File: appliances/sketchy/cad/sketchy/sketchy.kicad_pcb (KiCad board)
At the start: 2 copper layers, 6 parts, among them J1 Barrel_Jack, M1 Stepper_Motor_bipolar, M2 Stepper_Motor_bipolar, U1 ESP32PICO-KIT

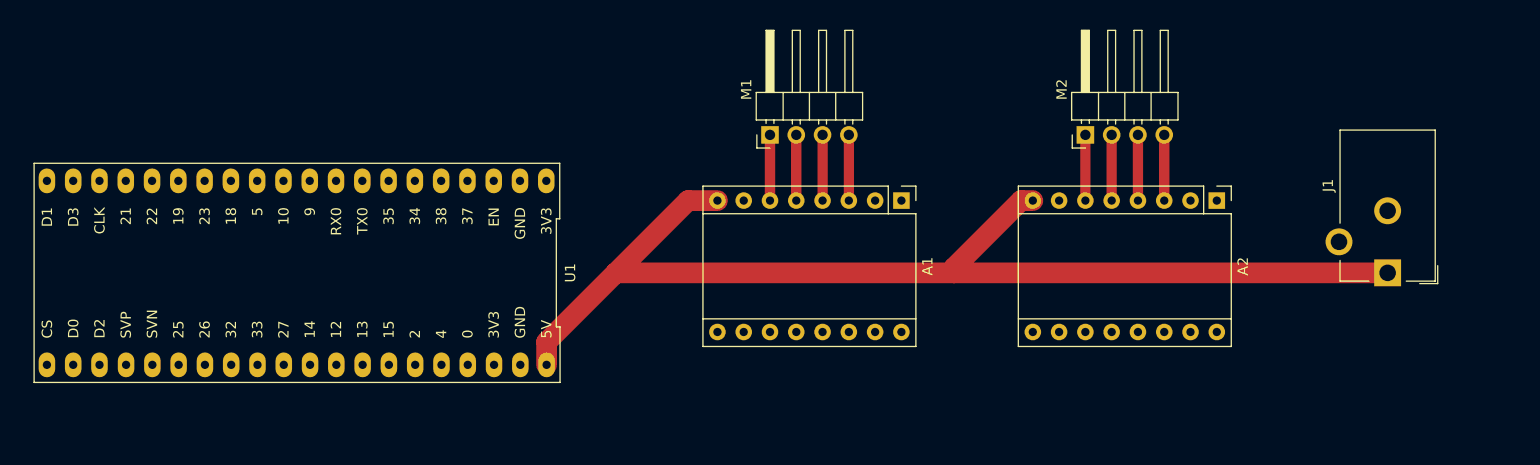
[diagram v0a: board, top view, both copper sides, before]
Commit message: Changed stepper driver to the 4988 that I'm actually using, routed all tracks, and added silkscreen text and mounting holes.
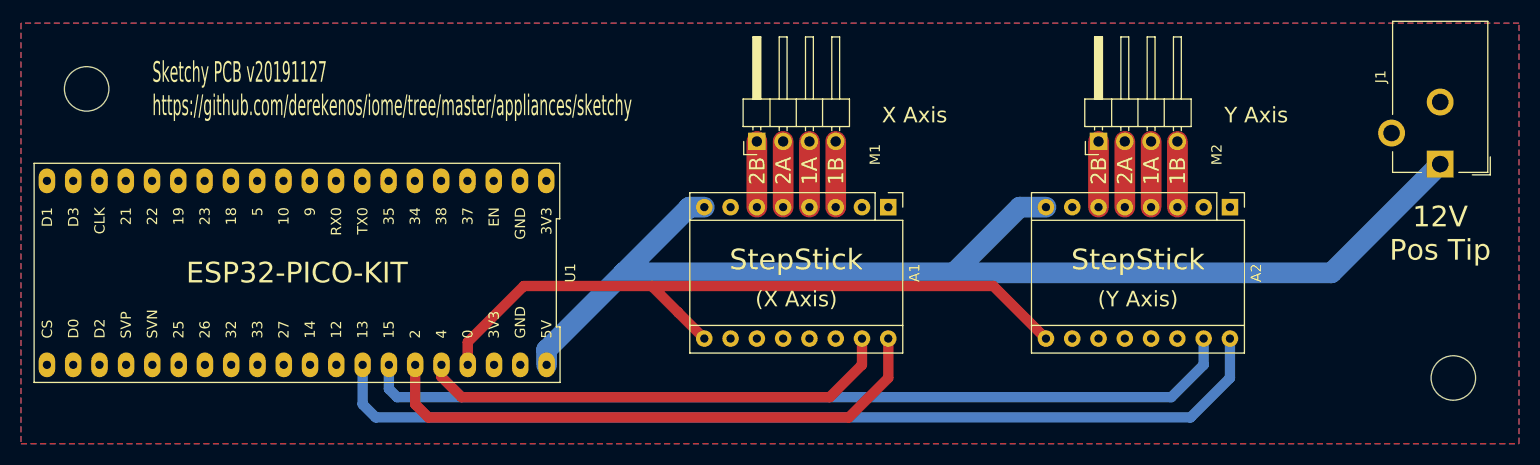
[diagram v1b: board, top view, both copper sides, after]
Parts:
- added REF**: MountingHole_4.3mm_M4, Mounting_Holes:MountingHole_4.3mm_M4, F.Cu at (195.6, 86.4)
- added REF**: MountingHole_4.3mm_M4, Mounting_Holes:MountingHole_4.3mm_M4, F.Cu at (63.5, 58.4)
- A1, A2: value Pololu_Breakout_DRV8825 -> Pololu_Breakout_A4988
- U1: value ESP32PICO-KIT -> ESP32-PICO-KIT
- moved J1 11.7 mm to (194.3, 65.7)
- moved A1 1.42 mm to (141.0, 69.8)
- moved A2 1.42 mm to (174.0, 69.8)
- moved M1 1.42 mm to (128.3, 63.5)
- moved M2 1.42 mm to (161.3, 63.5)
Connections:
- U1 pad 33: NOT_ENABLE -> STEPPER_Y_DIR
- U1 pad 34: STEPPER_X_STEP -> STEPPER_Y_STEP
- U1 pad 36: STEPPER_Y_STEP -> STEPPER_X_STEP
- U1 pad 37: STEPPER_Y_DIR -> NOT_ENABLE
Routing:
- net STEPPER_Y_DIR: track 0.00 -> 93.5 mm
- net STEPPER_Y_STEP: track 0.00 -> 85.2 mm
- net NOT_ENABLE: track 0.00 -> 69.6 mm
- net STEPPER_X_DIR: track 0.00 -> 55.4 mm
- net STEPPER_X_STEP: track 0.00 -> 46.5 mm
- net VDD: track 109.8 -> 117.2 mm
- added copper zone on B.Cu, net 3V3
- added copper zone on F.Cu, net GND
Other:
- board text added: "(X Axis)"
- board text added: "(Y Axis)"
- board text added: "12V Pos Tip"
- board text added: "1A"
- board text added: "1B"
- board text added: "2A"
- board text added: "2B"
- board text added: "Sketchy PCB v20191127 https://github.com/derekenos/iome/tree/master/appliances/sketchy"
- board text added: "StepStick"
- board text added: "X Axis"
- board text added: "Y Axis"

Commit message: Created denser (v2) PCB
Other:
- board outline added: 144.8 x 40.6 mm
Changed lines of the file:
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@@
   (general
     (thickness 1.6)
-    (drawings 16)
+    (drawings 20)
     (tracks 46)
     (modules 8)
@@
   (layers
     (0 "F.Cu" signal)
-    (31 "B.Cu" signal)
-    (32 "B.Adhes" user)
-    (33 "F.Adhes" user)
-    (34 "B.Paste" user)
-    (35 "F.Paste" user)
-    (36 "B.SilkS" user)
-    (37 "F.SilkS" user)
-    (38 "B.Mask" user)
-    (39 "F.Mask" user)
-    (40 "Dwgs.User" user)
-    (41 "Cmts.User" user)
-    (42 "Eco1.User" user)
-    (43 "Eco2.User" user)
+    (31 "B.Cu" signal hide)
+    (32 "B.Adhes" user hide)
+    (33 "F.Adhes" user hide)
+    (34 "B.Paste" user hide)
+    (35 "F.Paste" user hide)
+    (36 "B.SilkS" user hide)
+    (37 "F.SilkS" user hide)
+    (38 "B.Mask" user hide)
+    (39 "F.Mask" user hide)
+    (40 "Dwgs.User" user hide)
+    (41 "Cmts.User" user hide)
+    (42 "Eco1.User" user hide)
+    (43 "Eco2.User" user hide)
     (44 "Edge.Cuts" user)
-    (45 "Margin" user)
-    (46 "B.CrtYd" user)
-    (47 "F.CrtYd" user)
-    (48 "B.Fab" user)
-    (49 "F.Fab" user)
+    (45 "Margin" user hide)
+    (46 "B.CrtYd" user hide)
+    (47 "F.CrtYd" user hide)
+    (48 "B.Fab" user hide)
+    (49 "F.Fab" user hide)
   )
   (setup
@@
       (dielectric_constraints no)
     )
-    (last_trace_width 1)
+    (last_trace_width 0.25)
     (user_trace_width 1)
     (trace_clearance 0.2)
@@
     )
   )
+  (gr_line (start 201.93 52.07) (end 57.15 52.07) (layer "Edge.Cuts") (width 0.05))
+  (gr_line (start 201.93 92.71) (end 201.93 52.07) (layer "Edge.Cuts") (width 0.05))
+  (gr_line (start 57.15 92.71) (end 201.93 92.71) (layer "Edge.Cuts") (width 0.05))
+  (gr_line (start 57.15 52.07) (end 57.15 92.71) (layer "Edge.Cuts") (width 0.05))
   (gr_text "(Y Axis)" (at 165.1 78.74) (layer "F.SilkS")
     (effects (font (size 1.5 1.5) (thickness 0.3)))
